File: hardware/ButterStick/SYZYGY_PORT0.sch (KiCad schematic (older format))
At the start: 2 parts, among them U3 ECP5U25

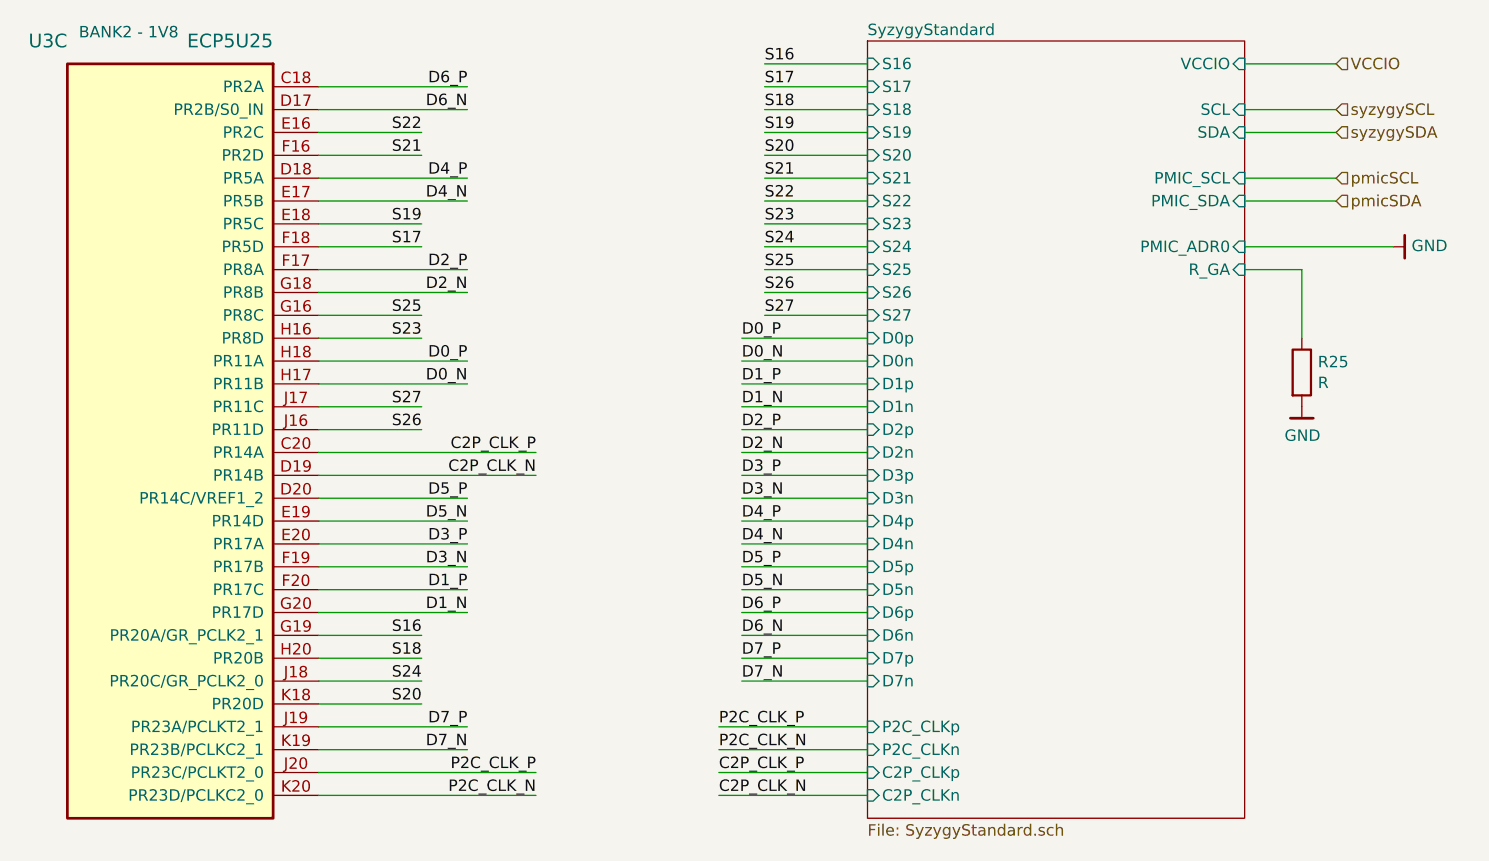
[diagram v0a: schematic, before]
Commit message: Routed all SYZYGY ports. Placed decoupling caps etc.
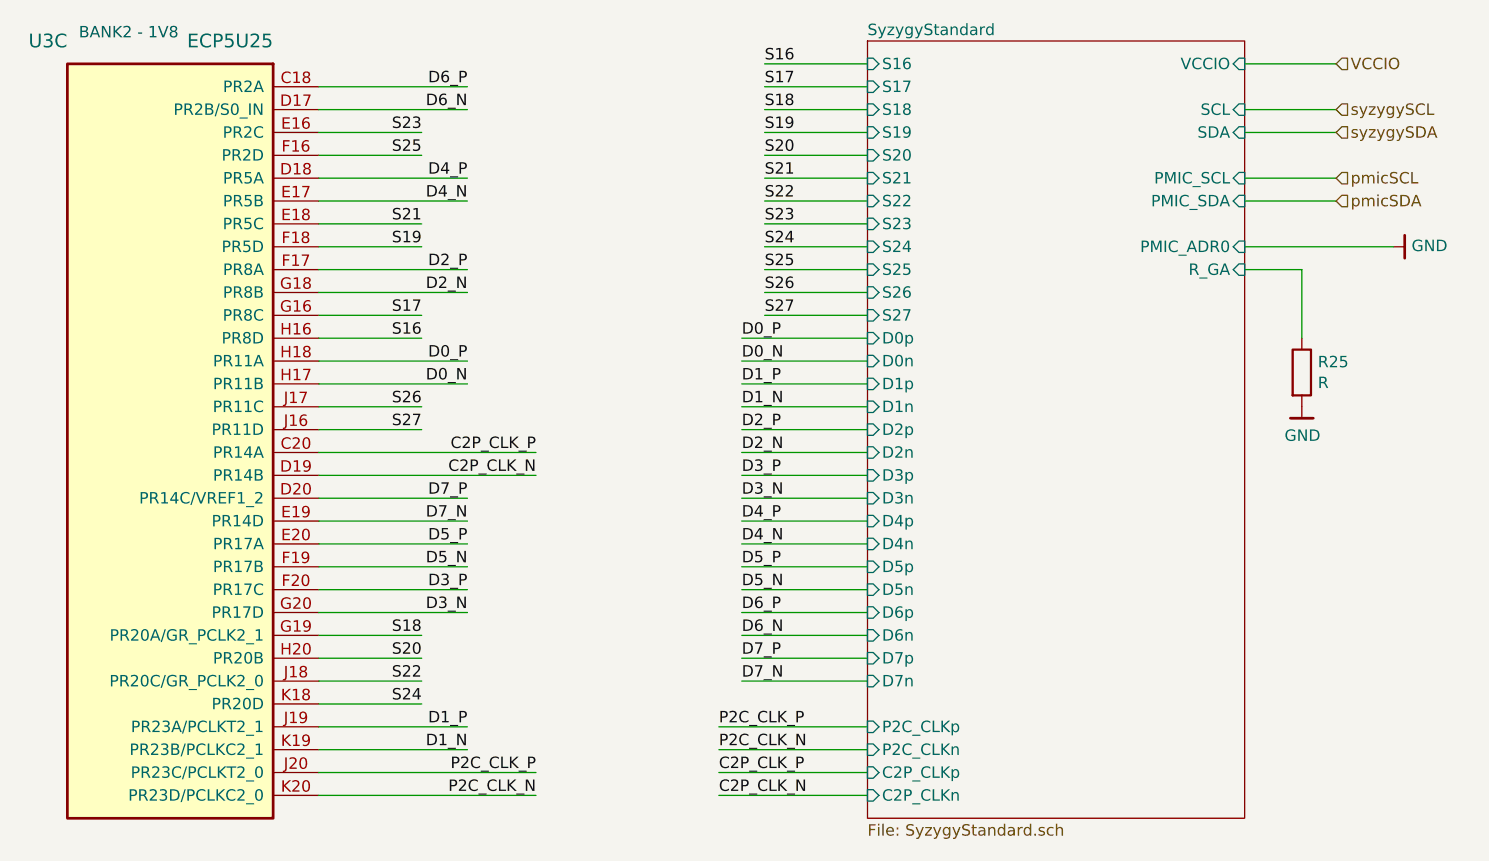
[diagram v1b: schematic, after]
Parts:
- R25: footprint (none) -> pkl_dipol:R_0402
- U3: footprint (none) -> gkl_housings_bga:caBGA_381_17x17
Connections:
- net D1_N: now also U3.K19 (PR23B/PCLKC2_1); no longer U3.G20 (PR17D)
- net D1_P: now also U3.J19 (PR23A/PCLKT2_1); no longer U3.F20 (PR17C)
- net D3_N: now also U3.G20 (PR17D); no longer U3.F19 (PR17B)
- net D3_P: now also U3.F20 (PR17C); no longer U3.E20 (PR17A)
- net D5_N: now also U3.F19 (PR17B); no longer U3.E19 (PR14D)
- net D5_P: now also U3.E20 (PR17A); no longer U3.D20 (PR14C/VREF1_2)
- net D7_N: now also U3.E19 (PR14D); no longer U3.K19 (PR23B/PCLKC2_1)
- net D7_P: now also U3.D20 (PR14C/VREF1_2); no longer U3.J19 (PR23A/PCLKT2_1)
- net S16: now also U3.H16 (PR8D); no longer U3.G19 (PR20A/GR_PCLK2_1)
- net S17: now also U3.G16 (PR8C); no longer U3.F18 (PR5D)
- net S18: now also U3.G19 (PR20A/GR_PCLK2_1); no longer U3.H20 (PR20B)
- net S19: now also U3.F18 (PR5D); no longer U3.E18 (PR5C)
- net S20: now also U3.H20 (PR20B); no longer U3.K18 (PR20D)
- net S21: now also U3.E18 (PR5C); no longer U3.F16 (PR2D)
- net S22: now also U3.J18 (PR20C/GR_PCLK2_0); no longer U3.E16 (PR2C)
- net S23: now also U3.E16 (PR2C); no longer U3.H16 (PR8D)
- net S24: now also U3.K18 (PR20D); no longer U3.J18 (PR20C/GR_PCLK2_0)
- net S25: now also U3.F16 (PR2D); no longer U3.G16 (PR8C)
- net S26: now also U3.J17 (PR11C); no longer U3.J16 (PR11D)
- net S27: now also U3.J16 (PR11D); no longer U3.J17 (PR11C)
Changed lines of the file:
@@
 $Descr A4 11693 8268
 encoding utf-8
-Sheet 8 13
+Sheet 8 14
 Title ""
 Date ""
@@
 F 0 "U3" H 5700 2800 60  0000 L CNN
 F 1 "ECP5U25" H 4800 2800 60  0000 L CNN
-F 2 "" H 4600 2600 50  0001 C CNN
+F 2 "gkl_housings_bga:caBGA_381_17x17" H 4600 2600 50  0001 C CNN
 F 3 "" H 4600 2600 50  0001 C CNN
 F 4 " 220-2052-ND " H -1650 1750 50  0001 C CNN "SN-DK"
@@
 C2P_CLK_N
 Wire Wire Line
+	4600 3700 5050 3700
+Wire Wire Line
+	4600 3600 5050 3600
+Wire Wire Line
 	4600 5000 5050 5000
 Wire Wire Line
@@
 	4600 3200 5050 3200
 Wire Wire Line
+	4600 5200 5050 5200
+Wire Wire Line
+	4600 2800 5050 2800
+Wire Wire Line
 	4600 5300 5050 5300
 Wire Wire Line
 	4600 2900 5050 2900
 Wire Wire Line
-	4600 2800 5050 2800
-Wire Wire Line
-	4600 3700 5050 3700
-Wire Wire Line
-	4600 5200 5050 5200
-Wire Wire Line
-	4600 3600 5050 3600
+	4600 4000 5050 4000
 Wire Wire Line
 	4600 4100 5050 4100
 Wire Wire Line
-	4600 4000 5050 4000
-Wire Wire Line
 	4600 3800 5250 3800
 Wire Wire Line
 	4600 3900 5250 3900
 Wire Wire Line
+	4600 5400 5250 5400
+Wire Wire Line
+	4600 5500 5250 5500
+Wire Wire Line
+	4600 3400 5250 3400
+Wire Wire Line
+	4600 3500 5250 3500
+Wire Wire Line
 	4600 4800 5250 4800
 Wire Wire Line
 	4600 4900 5250 4900
 Wire Wire Line
-	4600 3400 5250 3400
-Wire Wire Line
-	4600 3500 5250 3500
+	4600 3000 5250 3000
+Wire Wire Line
+	4600 3100 5250 3100
 Wire Wire Line
 	4600 4600 5250 4600
@@
 	4600 4700 5250 4700
 Wire Wire Line
-	4600 3000 5250 3000
-Wire Wire Line
-	4600 3100 5250 3100
+	4600 2600 5250 2600
+Wire Wire Line
+	4600 2700 5250 2700
 Wire Wire Line
 	4600 4400 5250 4400
@@
 	4600 4500 5250 4500
 Wire Wire Line
-	4600 2600 5250 2600
-Wire Wire Line
-	4600 2700 5250 2700
-Wire Wire Line
-	4600 5400 5250 5400
-Wire Wire Line
-	4600 5500 5250 5500
-Wire Wire Line
 	4600 5600 5550 5600
 Wire Wire Line
@@
 Wire Wire Line
 	4600 4300 5550 4300
+Text Label 5050 3700 2    50   ~ 0
+S16
+Text Label 5050 3600 2    50   ~ 0
+S17
 Text Label 5050 5000 2    50   ~ 0
-S16
+S18
 Text Label 5050 3300 2    50   ~ 0
-S17
+S19
 Text Label 5050 5100 2    50   ~ 0
-S18
+S20
 Text Label 5050 3200 2    50   ~ 0
-S19
+S21
+Text Label 5050 5200 2    50   ~ 0
+S22
+Text Label 5050 2800 2    50   ~ 0
+S23
 Text Label 5050 5300 2    50   ~ 0
-S20
+S24
 Text Label 5050 2900 2    50   ~ 0
-S21
-Text Label 5050 2800 2    50   ~ 0
-S22
-Text Label 5050 3700 2    50   ~ 0
-S23
-Text Label 5050 5200 2    50   ~ 0
-S24
-Text Label 5050 3600 2    50   ~ 0
 S25
+Text Label 5050 4000 2    50   ~ 0
+S26
 Text Label 5050 4100 2    50   ~ 0
-S26
-Text Label 5050 4000 2    50   ~ 0
 S27
 Text Label 5250 3800 2    50   ~ 0
@@
 Text Label 5250 3900 2    50   ~ 0
 D0_N
-Text Label 5250 4800 2    50   ~ 0
+Text Label 5250 5400 2    50   ~ 0
 D1_P
-Text Label 5250 4900 2    50   ~ 0
+Text Label 5250 5500 2    50   ~ 0
 D1_N
 Text Label 5250 3400 2    50   ~ 0
@@
 Text Label 5250 3500 2    50   ~ 0
 D2_N
-Text Label 5250 4600 2    50   ~ 0
+Text Label 5250 4800 2    50   ~ 0
 D3_P
-Text Label 5250 4700 2    50   ~ 0
+Text Label 5250 4900 2    50   ~ 0
 D3_N
 Text Label 5250 3000 2    50   ~ 0
@@
 Text Label 5250 3100 2    50   ~ 0
 D4_N
-Text Label 5250 4400 2    50   ~ 0
+Text Label 5250 4600 2    50   ~ 0
 D5_P
-Text Label 5250 4500 2    50   ~ 0
+Text Label 5250 4700 2    50   ~ 0
 D5_N
 Text Label 5250 2600 2    50   ~ 0
@@
 Text Label 5250 2700 2    50   ~ 0
 D6_N
-Text Label 5250 5400 2    50   ~ 0
+Text Label 5250 4400 2    50   ~ 0
 D7_P
-Text Label 5250 5500 2    50   ~ 0
+Text Label 5250 4500 2    50   ~ 0
 D7_N
 Text Label 5550 5600 2    50   ~ 0
@@
 F 0 "R25" H 8970 3896 50  0000 L CNN
 F 1 "R" H 8970 3805 50  0000 L CNN
-F 2 "" V 8830 3850 50  0001 C CNN
+F 2 "pkl_dipol:R_0402" V 8830 3850 50  0001 C CNN
 F 3 "~" H 8900 3850 50  0001 C CNN
 	1    8900 3850

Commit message: Added ESD on SD card signals.
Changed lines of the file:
@@
 $Descr A4 11693 8268
 encoding utf-8
-Sheet 8 14
+Sheet 8 13
 Title ""
 Date ""
@@
 	1    0    0    -1
 $EndComp
-$Comp
-L gkl_power:GND #PWR?
-U 1 1 5C99D197
-P 9300 3300
-AR Path="/5C80F1A0/5C99D197" Ref="#PWR?"  Part="1"
-AR Path="/5C80F19A/5C99D197" Ref="#PWR0213"  Part="1"
-F 0 "#PWR0213" H 9300 3050 50  0001 C CNN
-F 1 "GND" V 9304 3220 50  0000 R CNN
-F 2 "" H 9200 2950 50  0001 C CNN
-F 3 "" H 9300 3300 50  0001 C CNN
-	1    9300 3300
-	0    -1   -1   0
-$EndComp
 Wire Wire Line
 	8650 3300 9300 3300
@@
 Text HLabel 9050 3100 2    50   Input ~ 0
 pmicSDA
+$Comp
+L gkl_power:+3V3 #PWR0213
+U 1 1 5CD0E4BA
+P 9300 3300
+F 0 "#PWR0213" H 9300 3150 50  0001 C CNN
+F 1 "+3V3" V 9303 3406 50  0000 L CNN
+F 2 "" H 9300 3300 50  0001 C CNN
+F 3 "" H 9300 3300 50  0001 C CNN
+	1    9300 3300
+	0    1    1    0
+$EndComp
 $EndSCHEMATC

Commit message: Finished initial routing of PCB.. Most parts are finished.
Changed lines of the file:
@@
 $Descr A4 11693 8268
 encoding utf-8
-Sheet 8 13
+Sheet 7 13
 Title ""
 Date ""
@@
 F39 "VCCIO" I R 8650 2500 50
 F40 "R_GA" I R 8650 3400 50
+F41 "PMIC_EN" I R 8650 2600 50
 $EndSheet
 Wire Wire Line
@@
 	0    1    1    0
 $EndComp
+Wire Wire Line
+	8650 2600 9050 2600
+Text HLabel 9050 2600 2    50   Input ~ 0
+EN
 $EndSCHEMATC

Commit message: Update KiCad PCB.
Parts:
- U3: PN LFE5U-25F-6BG381I -> LFE5U-45F-8BG381C
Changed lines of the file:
@@
 F 3 "" H 4600 2600 50  0001 C CNN
 F 4 " 220-2052-ND " H -1650 1750 50  0001 C CNN "SN-DK"
-F 5 " LFE5U-25F-6BG381I " H -1650 1750 50  0001 C CNN "PN"
+F 5 "LFE5U-45F-8BG381C" H -1650 1750 50  0001 C CNN "PN"
 F 6 "Lattice" H -1650 1750 50  0001 C CNN "Mfg"
 	3    4600 2600

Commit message: Finalised part values update BOM values to reflect. Swapped layers 4/5 due to stackup changes
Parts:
- R25: value R -> 210k; Mfg (none) -> Stackpole Electronics Inc; PN (none) -> RMCF0402FT210K; Tol (none) -> 1%
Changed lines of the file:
@@
 EESchema Schematic File Version 4
 LIBS:ButterStick-cache
-EELAYER 26 0
+EELAYER 29 0
 EELAYER END
 $Descr A4 11693 8268
 encoding utf-8
-Sheet 7 13
-Title ""
-Date ""
-Rev ""
-Comp ""
+Sheet 9 13
+Title "ButterStick"
+Date "2019-03-19"
+Rev "r0_1"
+Comp "GsD"
 Comment1 ""
 Comment2 ""
@@
 AR Path="/5C80F19A/5C99D18A" Ref="R25"  Part="1"
 F 0 "R25" H 8970 3896 50  0000 L CNN
-F 1 "R" H 8970 3805 50  0000 L CNN
+F 1 "210k" H 8970 3805 50  0000 L CNN
 F 2 "pkl_dipol:R_0402" V 8830 3850 50  0001 C CNN
 F 3 "~" H 8900 3850 50  0001 C CNN
+F 4 "Stackpole Electronics Inc" H 0   0   50  0001 C CNN "Mfg"
+F 5 "RMCF0402FT210K" H 0   0   50  0001 C CNN "PN"
+F 6 "1%" H 0   0   50  0001 C CNN "Tol"
 	1    8900 3850
 	1    0    0    -1
